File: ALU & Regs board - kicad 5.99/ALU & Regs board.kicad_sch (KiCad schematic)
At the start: 7 parts, among them U12 MC74ACT04DG, U13 MC74SCT00DG, U14 MC74ACT32DG, U19 MC74ACT08DG, U22 MC74ACT02DG

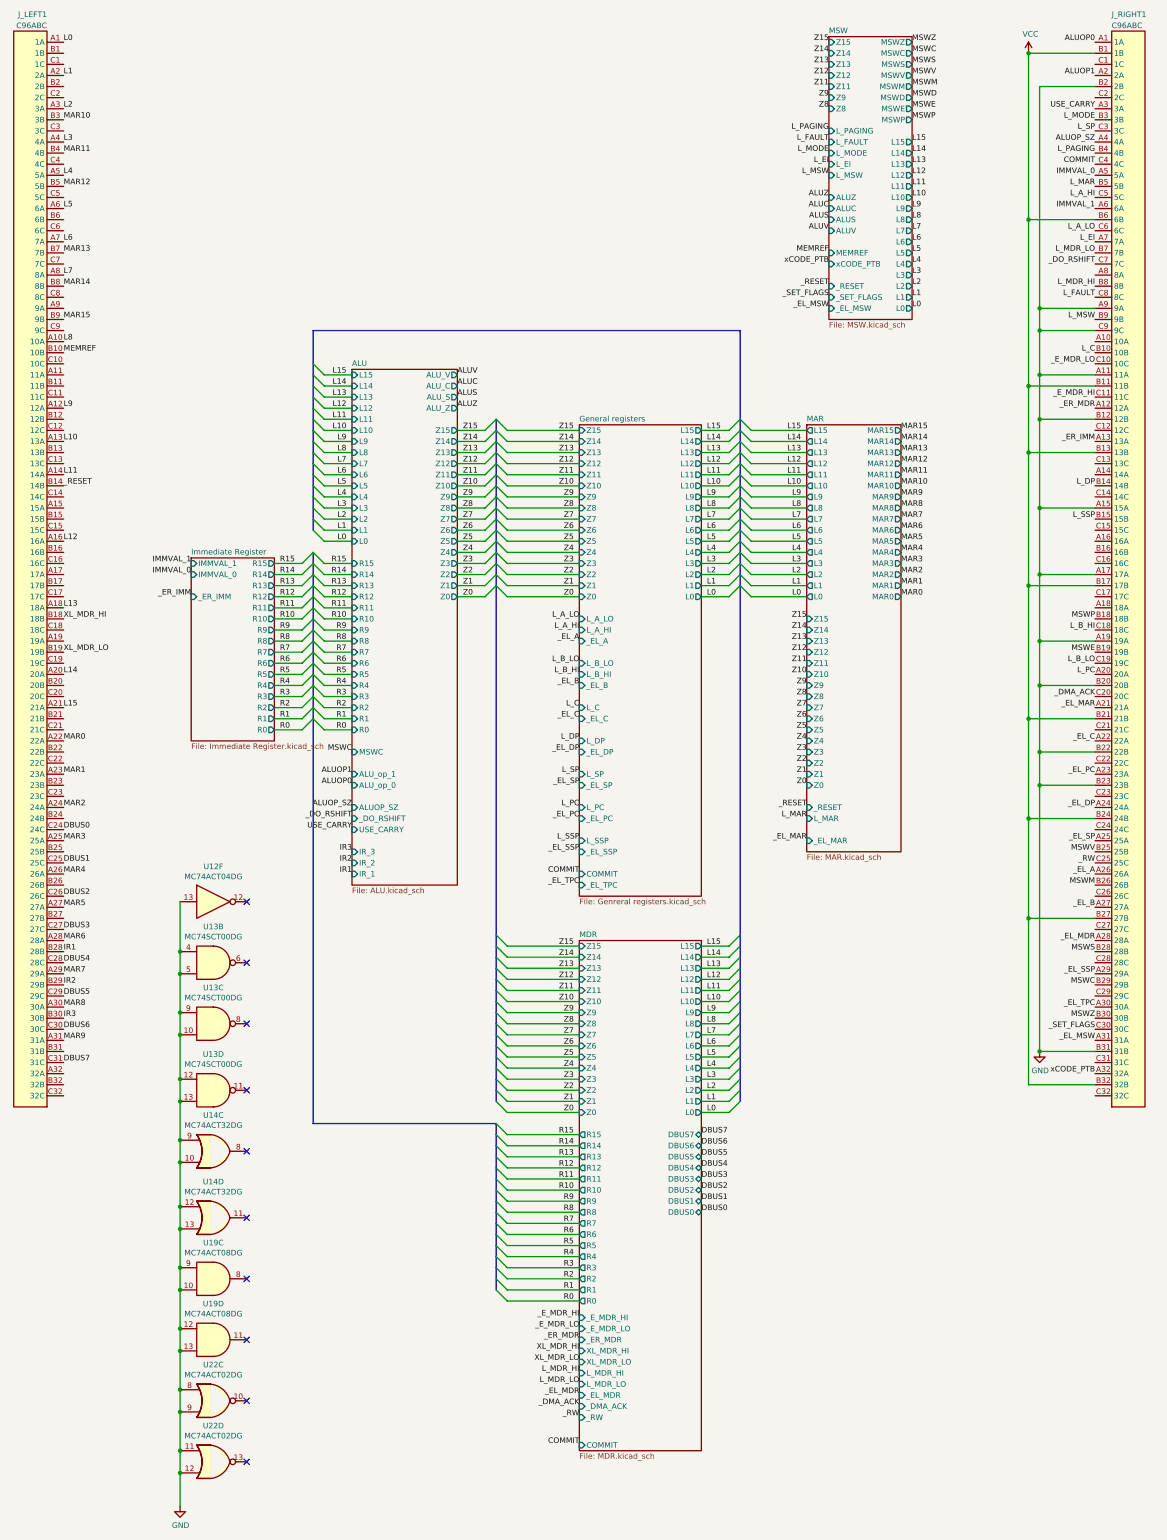
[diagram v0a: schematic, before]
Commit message: added a buffer on the _RESET line, which is rather loaded
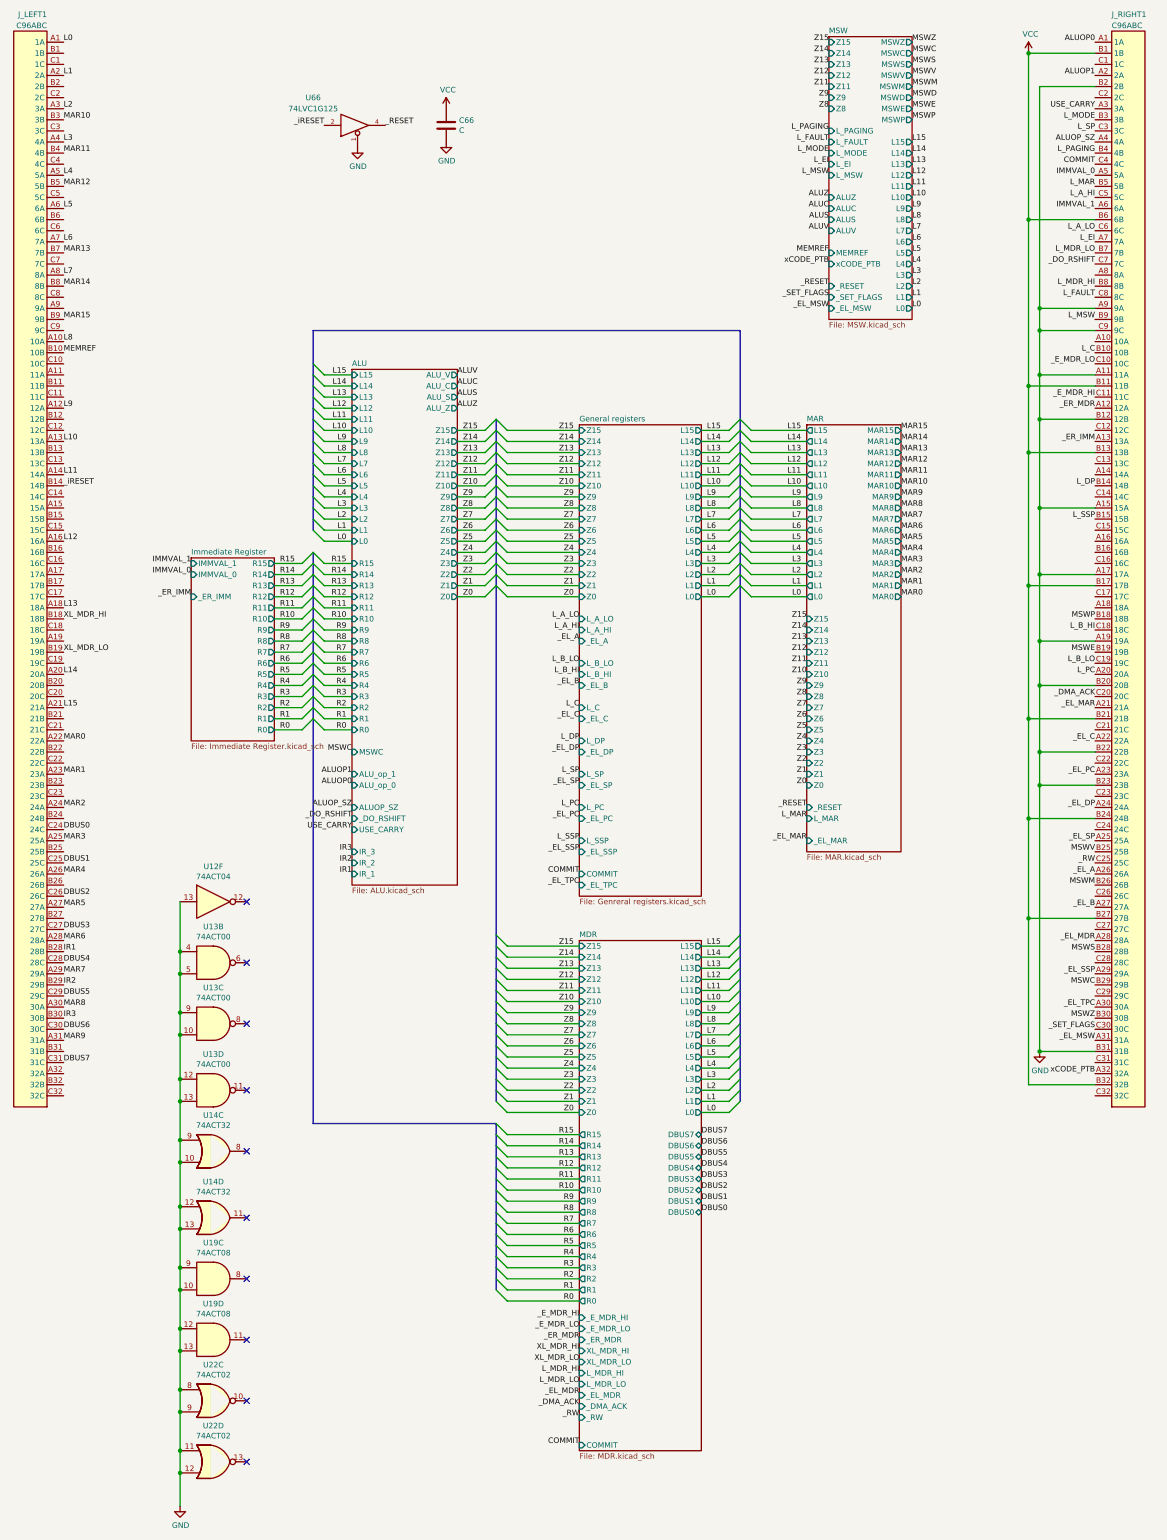
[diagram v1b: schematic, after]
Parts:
- added C66: C, Capacitor_SMD:C_1206_3216Metric, symbol Device:C
- added U66: 74LVC1G125, Package_TO_SOT_SMD:SOT-23-5, symbol 74xGxx:74LVC1G125
- U12: value MC74ACT04DG -> 74ACT04
- U13: value MC74SCT00DG -> 74ACT00
- U14: value MC74ACT32DG -> 74ACT32
- U19: value MC74ACT08DG -> 74ACT08
- U22: value MC74ACT02DG -> 74ACT02
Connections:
- net GND: now also C66.2, U66.1, U66.3 (GND)
- net VCC: now also C66.1, U66.5 (VCC)
- net _RESET: now also U66.4; no longer J_LEFT1.B14 (14B)
- new net _iRESET: J_LEFT1.B14 (14B), U66.2
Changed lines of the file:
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@@
   (junction (at 254 196.85) (diameter 1.016) (color 0 0 0 0))
   (junction (at 254 257.81) (diameter 1.016) (color 0 0 0 0))
+  (no_connect (at 72.39 323.85))
+  (no_connect (at 72.39 295.91))
   (no_connect (at 72.39 280.67))
+  (no_connect (at 72.39 266.7))
+  (no_connect (at 72.39 337.82))
   (no_connect (at 72.39 251.46))
+  (no_connect (at 72.39 351.79))
+  (no_connect (at 72.39 309.88))
   (no_connect (at 72.39 223.52))
-  (no_connect (at 72.39 323.85))
-  (no_connect (at 72.39 337.82))
   (no_connect (at 72.39 237.49))
-  (no_connect (at 72.39 266.7))
-  (no_connect (at 72.39 309.88))
-  (no_connect (at 72.39 295.91))
-  (no_connect (at 72.39 351.79))
   (bus_entry (at 85.09 146.05) (size 2.54 -2.54)
     (stroke (width 0.1524) (type solid) (color 0 0 0 0))
@@
     (effects (font (size 1.27 1.27)) (justify left bottom))
   )
-  (label "_RESET" (at 30.48 128.27 0)
+  (label "_iRESET" (at 30.48 128.27 0)
     (effects (font (size 1.27 1.27)) (justify left bottom))
   )
@@
     (effects (font (size 1.27 1.27)) (justify left bottom))
   )
+  (label "_iRESET" (at 90.17 45.72 180)
+    (effects (font (size 1.27 1.27)) (justify right bottom))
+  )
   (label "L15" (at 95.25 102.87 180)
     (effects (font (size 1.27 1.27)) (justify right bottom))
@@
     (effects (font (size 1.27 1.27)) (justify right bottom))
   )
+  (label "_RESET" (at 104.14 45.72 0)
+    (effects (font (size 1.27 1.27)) (justify left bottom))
+  )
   (label "ALUV" (at 120.65 102.87 0)
     (effects (font (size 1.27 1.27)) (justify left bottom))
@@
     (effects (font (size 1.27 1.27)) (justify right bottom))
   )
+  (symbol (lib_id "power:VCC") (at 118.11 41.91 0) (unit 1)
+    (in_bom yes) (on_board yes)
+    (property "Reference" "#PWR0109" (id 0) (at 118.11 45.72 0)
+      (effects (font (size 1.27 1.27)) hide)
+    )
+    (property "Value" "VCC" (id 1) (at 118.4783 37.5856 0))
+    (property "Footprint" "" (id 2) (at 118.11 41.91 0)
+      (effects (font (size 1.27 1.27)) hide)
+    )
+    (property "Datasheet" "" (id 3) (at 118.11 41.91 0)
+      (effects (font (size 1.27 1.27)) hide)
+    )
+  )
   (symbol (lib_id "power:VCC") (at 251.46 29.21 0) (unit 1)
     (in_bom yes) (on_board yes)
@@
     )
   )
+  (symbol (lib_id "power:GND") (at 97.79 50.8 0) (unit 1)
+    (in_bom yes) (on_board yes)
+    (property "Reference" "#PWR0107" (id 0) (at 97.79 57.15 0)
+      (effects (font (size 1.27 1.27)) hide)
+    )
+    (property "Value" "GND" (id 1) (at 97.9043 55.1244 0))
+    (property "Footprint" "" (id 2) (at 97.79 50.8 0)
+      (effects (font (size 1.27 1.27)) hide)
+    )
+    (property "Datasheet" "" (id 3) (at 97.79 50.8 0)
+      (effects (font (size 1.27 1.27)) hide)
+    )
+  )
+  (symbol (lib_id "power:GND") (at 118.11 49.53 0) (unit 1)
+    (in_bom yes) (on_board yes)
+    (property "Reference" "#PWR0108" (id 0) (at 118.11 55.88 0)
+      (effects (font (size 1.27 1.27)) hide)
+    )
+    (property "Value" "GND" (id 1) (at 118.2243 53.8544 0))
+    (property "Footprint" "" (id 2) (at 118.11 49.53 0)
+      (effects (font (size 1.27 1.27)) hide)
+    )
+    (property "Datasheet" "" (id 3) (at 118.11 49.53 0)
+      (effects (font (size 1.27 1.27)) hide)
+    )
+  )
   (symbol (lib_id "power:GND") (at 254 257.81 0) (unit 1)
     (in_bom yes) (on_board yes)
@@
     )
   )
+  (symbol (lib_id "Device:C") (at 118.11 45.72 0) (unit 1)
+    (in_bom yes) (on_board yes)
+    (property "Reference" "C66" (id 0) (at 121.031 44.571 0)
+      (effects (font (size 1.27 1.27)) (justify left))
+    )
+    (property "Value" "C" (id 1) (at 121.0311 46.8693 0)
+      (effects (font (size 1.27 1.27)) (justify left))
+    )
+    (property "Footprint" "Capacitor_SMD:C_1206_3216Metric" (id 2) (at 119.0752 49.53 0)
+      (effects (font (size 1.27 1.27)) hide)
+    )
+    (property "Datasheet" "~" (id 3) (at 118.11 45.72 0)
+      (effects (font (size 1.27 1.27)) hide)
+    )
+  )
+  (symbol (lib_id "74xGxx:74LVC1G125") (at 97.79 45.72 0) (mirror x) (unit 1)
+    (in_bom yes) (on_board yes)
+    (property "Reference" "U66" (id 0) (at 87.63 39.37 0))
+    (property "Value" "74LVC1G125" (id 1) (at 87.63 41.91 0))
+    (property "Footprint" "Package_TO_SOT_SMD:SOT-23-5" (id 2) (at 97.79 45.72 0)
+      (effects (font (size 1.27 1.27)) hide)
+    )
+    (property "Datasheet" "http://www.ti.com/lit/sg/scyt129e/scyt129e.pdf" (id 3) (at 97.79 45.72 0)
+      (effects (font (size 1.27 1.27)) hide)
+    )
+  )
   (symbol (lib_id "74xx:74LS04") (at 64.77 223.52 0) (unit 6)
     (in_bom yes) (on_board yes)
     (property "Reference" "U12" (id 0) (at 64.77 215.4682 0))
-    (property "Value" "MC74ACT04DG" (id 1) (at 64.77 217.7796 0))
+    (property "Value" "74ACT04" (id 1) (at 64.77 217.78 0))
     (property "Footprint" "Package_SO:SOIC-14_3.9x8.7mm_P1.27mm" (id 2) (at 64.77 223.52 0)
       (effects (font (size 1.27 1.27)) hide)
@@
     (in_bom yes) (on_board yes)
     (property "Reference" "U13" (id 0) (at 64.77 229.235 0))
-    (property "Value" "MC74SCT00DG" (id 1) (at 64.77 231.5464 0))
+    (property "Value" "74ACT00" (id 1) (at 64.77 231.546 0))
     (property "Footprint" "Package_SO:SOIC-14_3.9x8.7mm_P1.27mm" (id 2) (at 64.77 237.49 0)
       (effects (font (size 1.27 1.27)) hide)
@@
     (in_bom yes) (on_board yes)
     (property "Reference" "U13" (id 0) (at 64.77 243.205 0))
-    (property "Value" "MC74SCT00DG" (id 1) (at 64.77 245.5164 0))
+    (property "Value" "74ACT00" (id 1) (at 64.77 245.5164 0))
     (property "Footprint" "Package_SO:SOIC-14_3.9x8.7mm_P1.27mm" (id 2) (at 64.77 251.46 0)
       (effects (font (size 1.27 1.27)) hide)
@@
     (in_bom yes) (on_board yes)
     (property "Reference" "U13" (id 0) (at 64.77 258.445 0))
-    (property "Value" "MC74SCT00DG" (id 1) (at 64.77 260.7564 0))
+    (property "Value" "74ACT00" (id 1) (at 64.77 260.7564 0))
     (property "Footprint" "Package_SO:SOIC-14_3.9x8.7mm_P1.27mm" (id 2) (at 64.77 266.7 0)
       (effects (font (size 1.27 1.27)) hide)
@@
     (in_bom yes) (on_board yes)
     (property "Reference" "U14" (id 0) (at 64.77 272.415 0))
-    (property "Value" "MC74ACT32DG" (id 1) (at 64.77 274.7264 0))
+    (property "Value" "74ACT32" (id 1) (at 64.77 274.726 0))
     (property "Footprint" "Package_SO:SOIC-14_3.9x8.7mm_P1.27mm" (id 2) (at 64.77 280.67 0)
       (effects (font (size 1.27 1.27)) hide)
@@
     (in_bom yes) (on_board yes)
     (property "Reference" "U14" (id 0) (at 64.77 287.655 0))
-    (property "Value" "MC74ACT32DG" (id 1) (at 64.77 289.9664 0))
+    (property "Value" "74ACT32" (id 1) (at 64.77 289.9664 0))
     (property "Footprint" "Package_SO:SOIC-14_3.9x8.7mm_P1.27mm" (id 2) (at 64.77 295.91 0)
       (effects (font (size 1.27 1.27)) hide)
@@
     (in_bom yes) (on_board yes)
     (property "Reference" "U19" (id 0) (at 64.77 301.625 0))
-    (property "Value" "MC74ACT08DG" (id 1) (at 64.77 303.9364 0))
+    (property "Value" "74ACT08" (id 1) (at 64.77 303.936 0))
     (property "Footprint" "Package_SO:SOIC-14_3.9x8.7mm_P1.27mm" (id 2) (at 64.77 309.88 0)
       (effects (font (size 1.27 1.27)) hide)
@@
     (in_bom yes) (on_board yes)
     (property "Reference" "U19" (id 0) (at 64.77 315.595 0))
-    (property "Value" "MC74ACT08DG" (id 1) (at 64.77 317.9064 0))
+    (property "Value" "74ACT08" (id 1) (at 64.77 317.9064 0))
     (property "Footprint" "Package_SO:SOIC-14_3.9x8.7mm_P1.27mm" (id 2) (at 64.77 323.85 0)
       (effects (font (size 1.27 1.27)) hide)
@@
     (in_bom yes) (on_board yes)
     (property "Reference" "U22" (id 0) (at 64.77 329.565 0))
-    (property "Value" "MC74ACT02DG " (id 1) (at 64.77 331.8764 0))
+    (property "Value" "74ACT02" (id 1) (at 64.77 331.876 0))
     (property "Footprint" "Package_SO:SOIC-14_3.9x8.7mm_P1.27mm" (id 2) (at 64.77 337.82 0)
       (effects (font (size 1.27 1.27)) hide)
@@
     (in_bom yes) (on_board yes)
     (property "Reference" "U22" (id 0) (at 64.77 343.535 0))
-    (property "Value" "MC74ACT02DG " (id 1) (at 64.77 345.8464 0))
+    (property "Value" "74ACT02" (id 1) (at 64.77 345.8464 0))
     (property "Footprint" "Package_SO:SOIC-14_3.9x8.7mm_P1.27mm" (id 2) (at 64.77 351.79 0)
       (effects (font (size 1.27 1.27)) hide)
@@
   )
   (symbol_instances
+    (path "/e061c244-6848-40fa-b382-50b1946619a2"
+      (reference "#PWR0107") (unit 1)
+    )
+    (path "/7aa1998c-4f50-4695-bab5-3b6e81bb26e7"
+      (reference "#PWR0108") (unit 1)
+    )
+    (path "/aa6e9d4d-500f-4aca-8845-045930f2e93f"
+      (reference "#PWR0109") (unit 1)
+    )
     (path "/00000000-0000-0000-0000-00006098ca23"
       (reference "#PWR0261") (unit 1)
@@
       (reference "#PWR0263") (unit 1)
     )
+    (path "/dcce0d53-42a2-4fc5-acb2-9d5d91481967"
+      (reference "C66") (unit 1)
+    )
     (path "/00000000-0000-0000-0000-00005f547ccc"
       (reference "J_LEFT1") (unit 1)
@@
       (reference "U22") (unit 4)
     )
+    (path "/6ca3c692-0119-4b93-8f18-6e89b49d043b"
+      (reference "U66") (unit 1)
+    )
     (path "/00000000-0000-0000-0000-00005ff9c3ea/00000000-0000-0000-0000-00005ffa2add"
